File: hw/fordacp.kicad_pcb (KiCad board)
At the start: 2 copper layers, 81.9 x 42.4 mm, 35 parts, among them IC1 ATMEGA2560-A, P1 CONN_02X06, U1 SP3485CN, U2 AP1117D50, U3 BLK-MD-SPK-B, U4 XS3860, Y1 16MHz

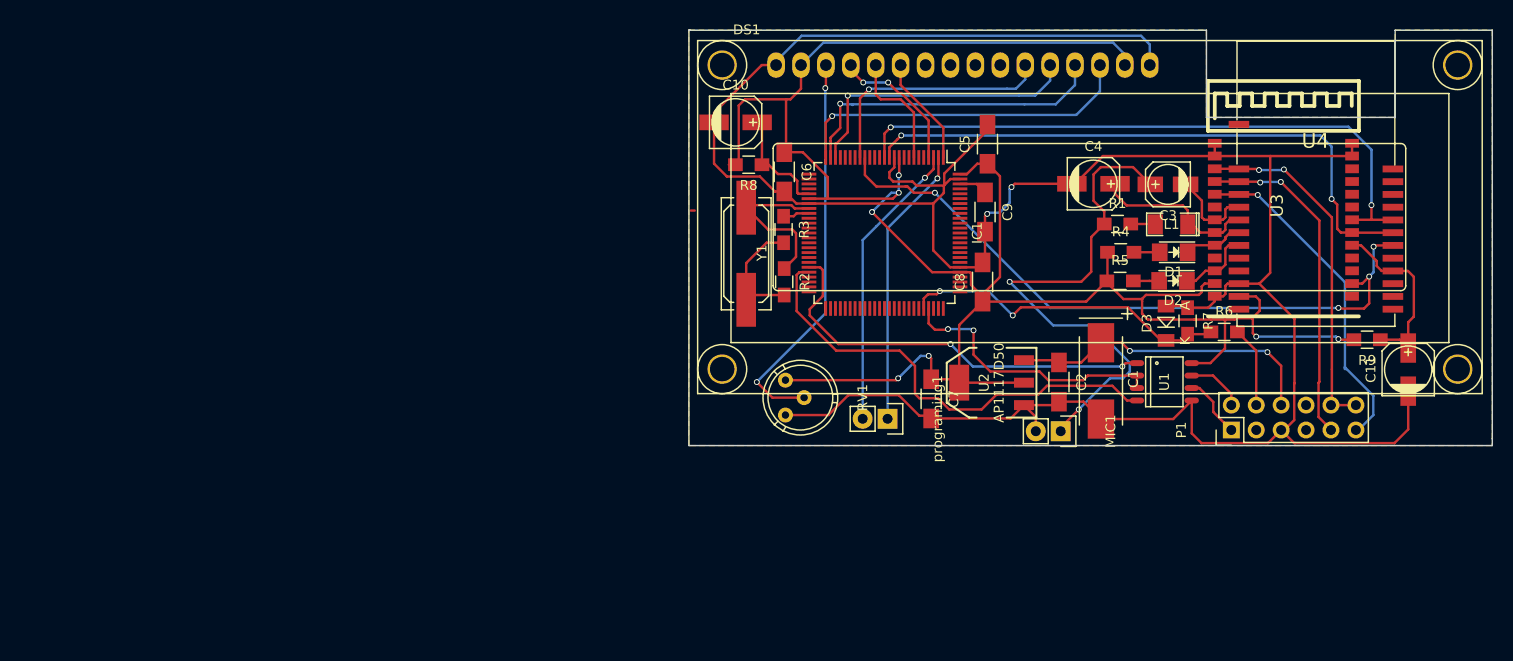
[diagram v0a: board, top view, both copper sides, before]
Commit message: set PCB witout LCD as default
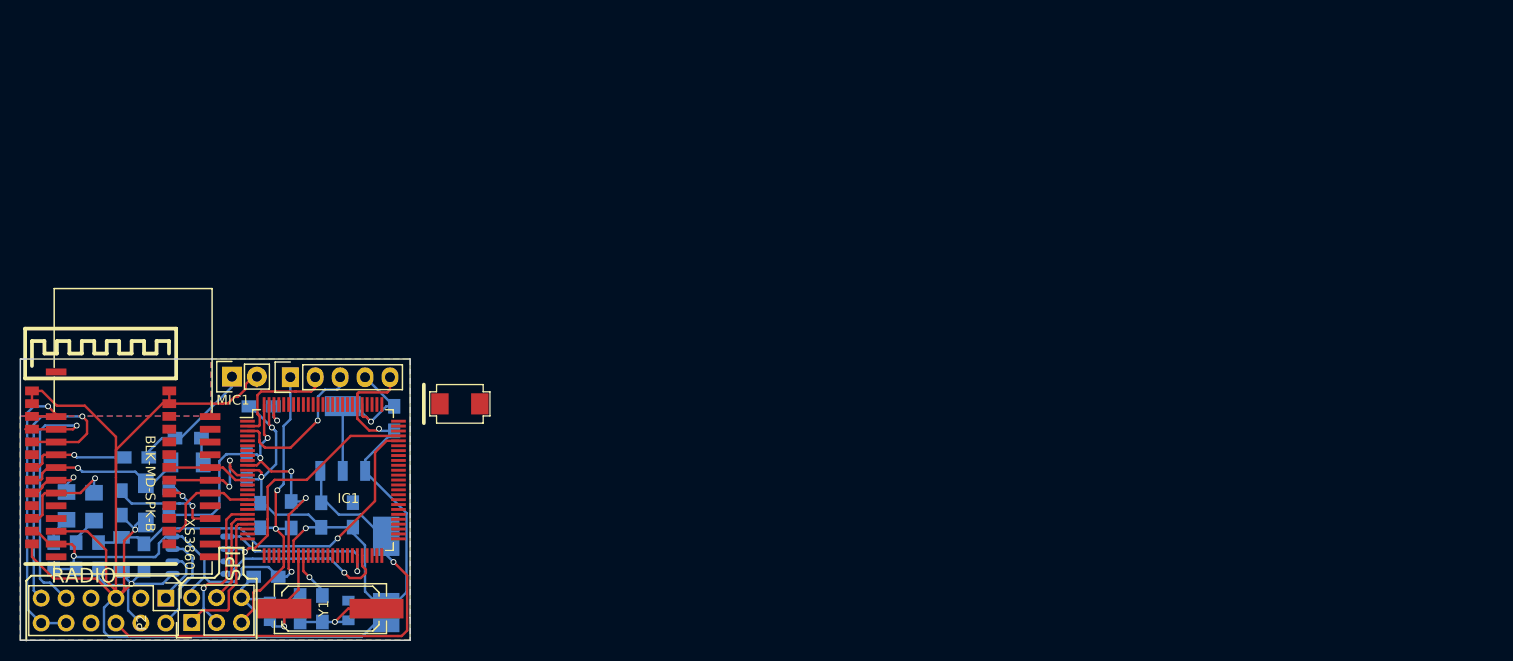
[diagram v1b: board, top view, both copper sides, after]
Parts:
- removed DS1: LCD-016N002L, WC1602A
- removed RV1: 1k, Potentiometers:Potentiometer_Bourns_3339H_Angular_ScrewUp
- added C12: 22, Capacitors_SMD:C_0805, B.Cu at (140.2, 114.1)
- added C13: 22, Capacitors_SMD:C_0805, B.Cu at (148.2, 114.0)
- added D4: 1N4007, do-214.mod:DO-214AA, F.Cu at (159.5, 93.0)
- added P2: CONN_02X03, Pin_Headers:Pin_Header_Straight_2x03, F.Cu at (132.2, 115.3)
- C1, D1, D2, D3, L1, R2, R3, R4, R5, R6, R7, U1, U2: moved to B.Cu
- C10, C11: value 2u2/10V -> 1u/16V; footprint Capacitors_SMD:c_elec_5x5.3 -> Capacitors_SMD:C_0805_HandSoldering; moved to B.Cu
- C2, C5, C6, C7, C8, C9: footprint Capacitors_SMD:C_1206_HandSoldering -> Capacitors_SMD:C_0805_HandSoldering; moved to B.Cu
- C3: footprint Capacitors_SMD:c_elec_4x5.3 -> Capacitors_SMD:C_0805_HandSoldering; moved to B.Cu
- C4: footprint Capacitors_SMD:c_elec_5x5.3 -> Capacitors_SMD:C_1206_HandSoldering; moved to B.Cu
- R1: value 2k7 -> 2k7(3k3); moved to B.Cu
- R8, R9: value 4k7 -> 10k; moved to B.Cu
- U4: value XS3860 -> XS3868
- programing1: value CONN_01X02 -> CONN_01X05; footprint Pin_Headers:Pin_Header_Straight_1x02 -> Pin_Headers:Pin_Header_Straight_1x05
- moved C11 131.9 mm to (125.0, 103.1), turned to 270 degrees
- moved R9 123.3 mm to (129.9, 102.9), turned to 270 degrees
- moved U4 123.2 mm to (118.4, 110.1)
- moved U3 123.2 mm to (114.6, 85.3)
- moved R6 117.0 mm to (122.7, 108.5), turned to 270 degrees
- moved D1 115.8 mm to (119.4, 103.4), turned to 270 degrees
- moved R4 113.1 mm to (118.1, 108.5), turned to 90 degrees
- moved D2 112.4 mm to (122.2, 103.4), turned to 270 degrees
- moved R5 110.1 mm to (120.4, 108.5), turned to 90 degrees
- moved P1 110.0 mm to (129.5, 112.8), turned to 270 degrees
- moved R7 109.1 mm to (127.3, 108.6), turned to 90 degrees
- moved D3 109.1 mm to (125.0, 108.3), turned to 270 degrees
- moved C3 108.8 mm to (126.6, 98.4)
- moved L1 103.3 mm to (131.7, 98.9), turned to 0 degrees
- moved C4 102.0 mm to (127.5, 103.1), turned to 270 degrees
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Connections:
- IC1 pad 20: (no net) -> /SCK
- IC1 pad 21: (no net) -> /MOSI
- IC1 pad 22: (no net) -> /MISO
- U2 pad VO: +5V -> Net-(D4-Pad2)
- programing1 pad 1: /RX0 -> /ARD_RESET
- programing1 pad 2: /TX0 -> /RX0
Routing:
- net +5V: track 219.5 -> 91.7 mm
- net /BT_WAKE: track 69.1 -> 11.1 mm, vias 4 -> 0
- net /BT_RX: track 64.7 -> 8.53 mm, vias 2 -> 0
- net GND: track 281.0 -> 226.7 mm, vias 2 -> 6
- net /BT_TX: track 61.6 -> 12.0 mm
- net Net-(DS1-Pad3): track 40.7 -> 0.00 mm, vias 2 -> 0
- net Net-(C3-Pad1): track 53.6 -> 12.9 mm, vias 2 -> 0
- net /LCD_D7: track 35.5 -> 0.00 mm, vias 1 -> 0
- net /LCD_D6: track 33.2 -> 0.00 mm, vias 1 -> 0
- net /LCD_D5: track 31.0 -> 0.00 mm, vias 1 -> 0
- net /RS485_DI: track 47.2 -> 18.3 mm, vias 0 -> 1
- net /LCD_D4: track 25.1 -> 0.00 mm, vias 1 -> 0
- net /RS485_R0: track 42.4 -> 17.3 mm, vias 2 -> 1
- net +12V: track 33.2 -> 52.6 mm, vias 2 -> 1
- net /ARD_RESET: track 12.0 -> 31.3 mm, vias 0 -> 2
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- added copper zone on B.Cu, net GND
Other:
- board size 81.9 x 42.4 mm -> 39.7 x 28.7 mm
- board text added: "5V"
- board text added: "BLK-MD-SPK-B"
- board text added: "GND"
- board text added: "MIC"
- board text added: "RADIO"
- board text added: "RST"
- board text added: "RX"
- board text added: "SPI"
- board text added: "TX"
- board text added: "XS3860"

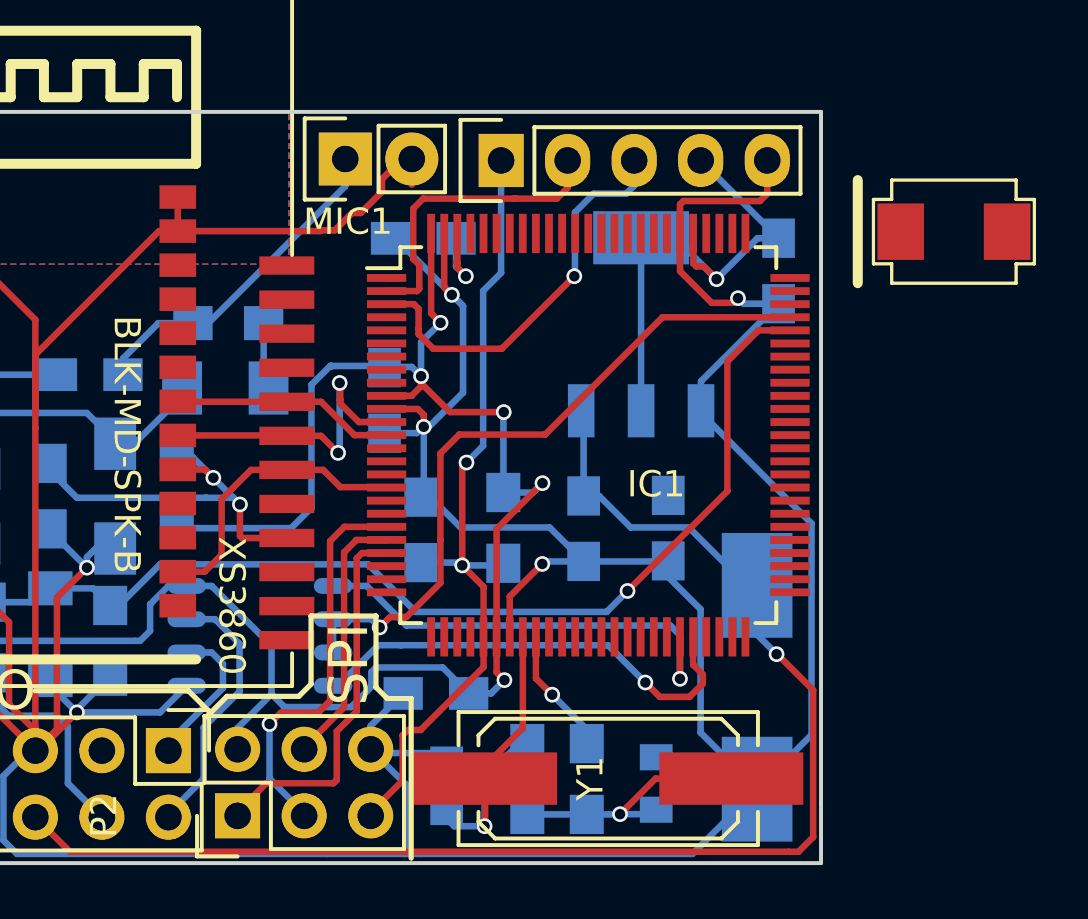
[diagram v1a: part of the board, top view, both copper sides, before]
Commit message: renam XS3860 to XS3868
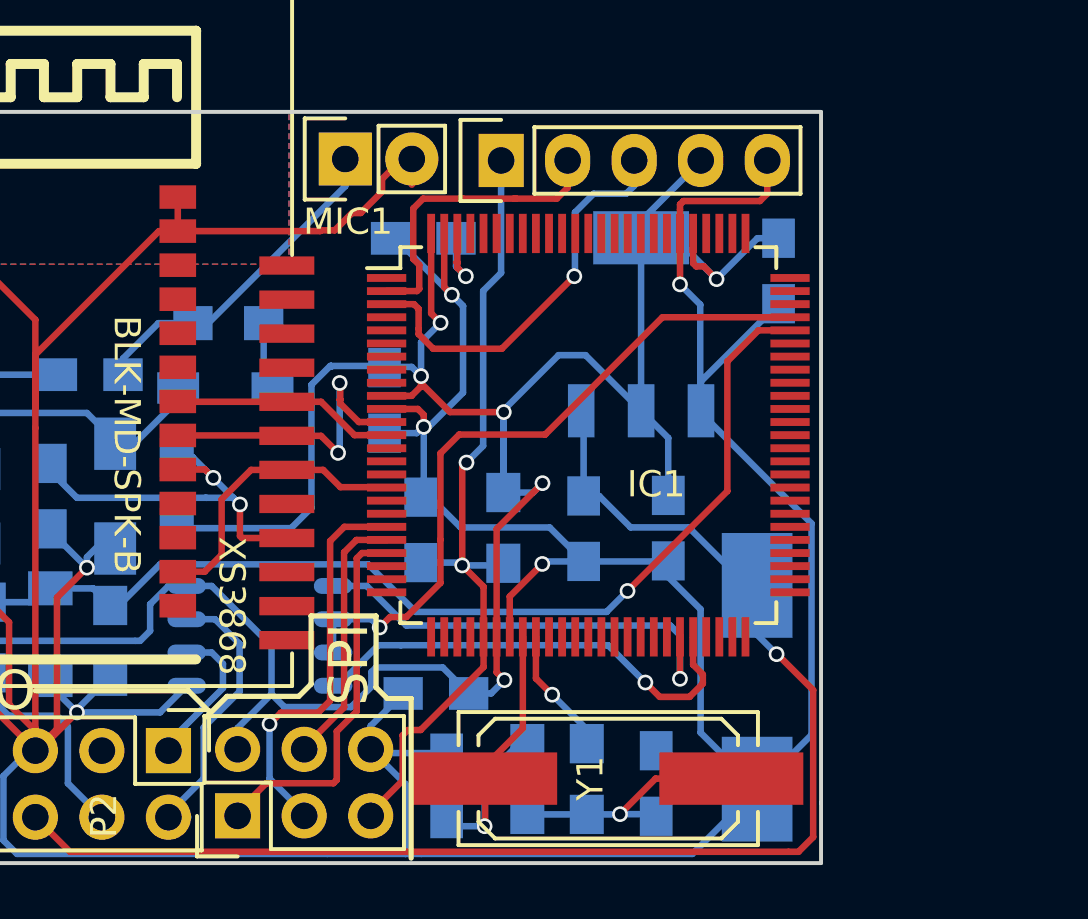
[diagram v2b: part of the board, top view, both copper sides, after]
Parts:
- removed D4: 1N4007, do-214.mod:DO-214AA
- C12, C13: footprint Capacitors_SMD:C_0805 -> Capacitors_SMD:C_0805_HandSoldering
- L1: footprint SMD_Packages:SMD-1206_Pol -> Choke_SMD:Choke_SMD_1206_Standard
- U4: value XS3868 -> XS3860
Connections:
- U2 pad VO: Net-(D4-Pad2) -> +5V
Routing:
- net +5V: track 91.7 -> 116.3 mm
- net Net-(D4-Pad2): track 11.8 -> 0.00 mm
- net GND: track 226.7 -> 227.8 mm
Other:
- board text added: "XS3868"
- board text removed: "XS3860"

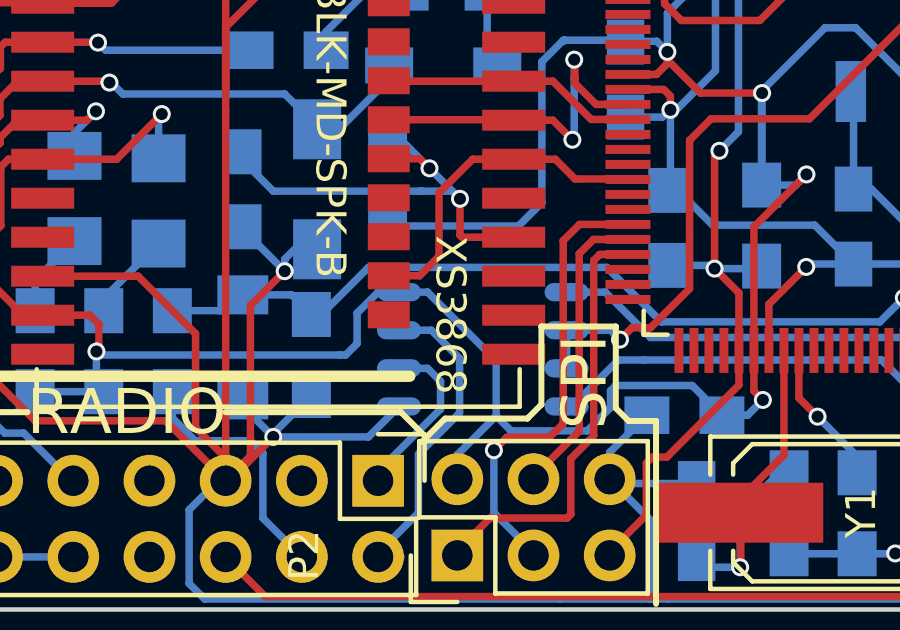
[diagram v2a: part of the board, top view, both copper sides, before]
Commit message: rename XS3868 to S3860M-S
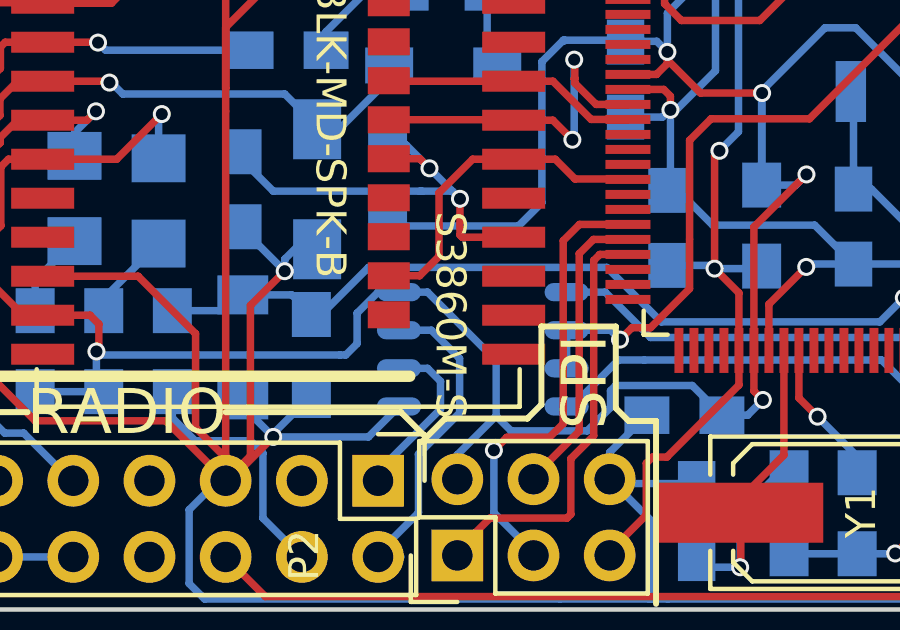
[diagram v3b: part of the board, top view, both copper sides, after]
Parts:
- U4: footprint my_modules:XS3868 -> my_modules:S3860M-S
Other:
- board text added: "S3860M-S"
- board text removed: "XS3868"
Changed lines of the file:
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@@
-(kicad_pcb (version 4) (host pcbnew 0.201512281231+6406~40~ubuntu14.04.1-stable)
+(kicad_pcb (version 4) (host pcbnew 0.201601061458+6427~40~ubuntu14.04.1-stable)
   (general
     (links 107)
@@
       (net 1 GND))
   )
-  (module my_modules:XS3868 (layer F.Cu)
+  (module my_modules:S3860M-S (layer F.Cu)
     (at 118.36066 110.1092)
     (fp_text reference U4 (at 7.8 -18.7) (layer F.SilkS) hide
@@
     (effects (font (size 1 1) (thickness 0.15)))
   )
-  (gr_text XS3868 (at 131.953 107.2515 270) (layer F.SilkS)
+  (gr_text S3860M-S (at 131.953 107.2515 270) (layer F.SilkS)
     (effects (font (size 1 1) (thickness 0.15)))
   )
